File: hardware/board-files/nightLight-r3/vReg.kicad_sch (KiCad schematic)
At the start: 15 parts, among them IC1 PAM2401SCADJ, Q1 NMOS, Q2 PMOS

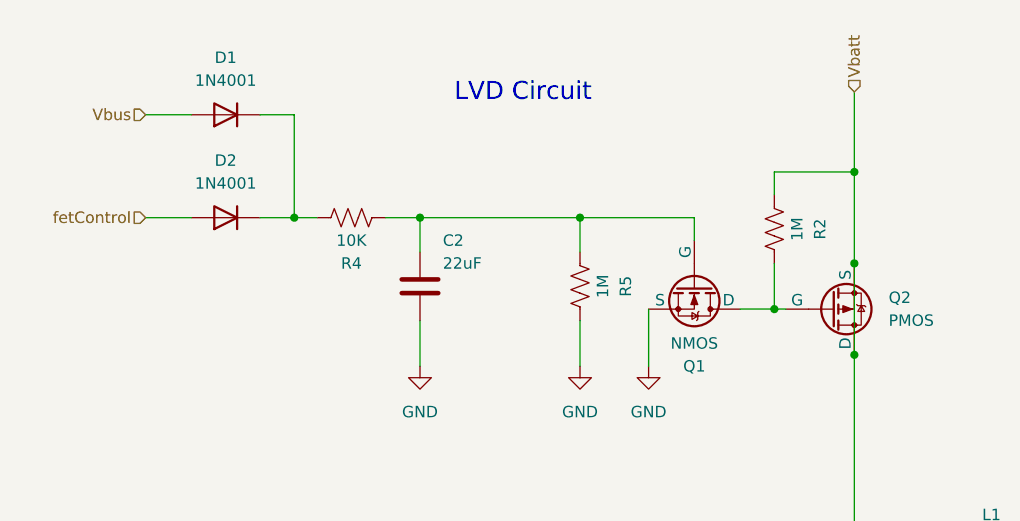
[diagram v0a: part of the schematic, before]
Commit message: finished shematic and added to PCB
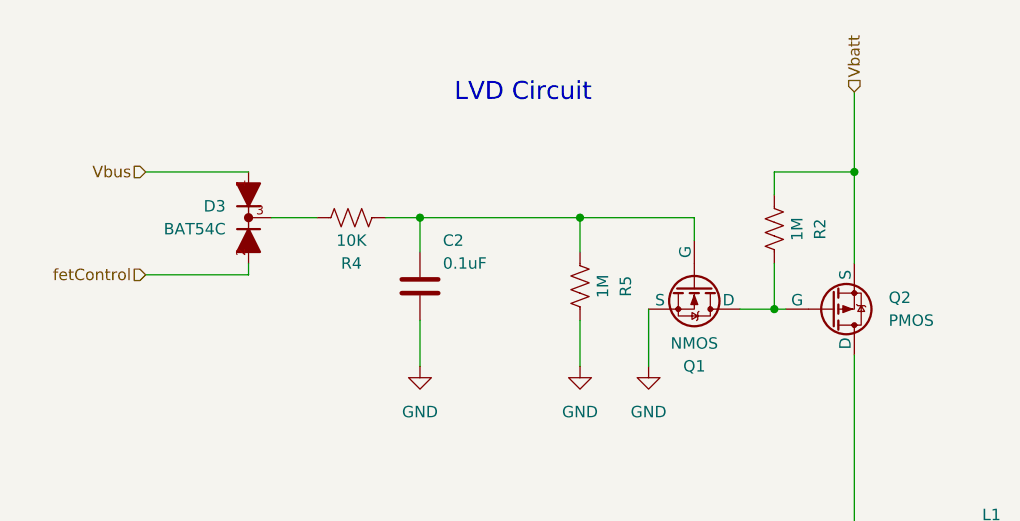
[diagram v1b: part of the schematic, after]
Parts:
- removed D1, D2: 1N4001, Diode_THT:D_DO-41_SOD81_P10.16mm_Horizontal, symbol Diode:1N4001
- added D3: BAT54C, BAT54C:SOT23-R, symbol BAT54C:BAT54C
- C2: value 22uF -> 0.1uF
- Q1: footprint (none) -> IRLML6402TRPBF:SOT95P237X112-3N
- Q2: footprint (none) -> IRLML6344TRPBF:SOT95P240X112-3N
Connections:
- net Vbatt: no longer C1.1, IC1.3 (VIN), L1.1, Q2.1 (D), R1.1
- net Vbus: now also D3.1
- net fetControl: now also D3.2
- net at R4.2: now also D3.3
- new net: C1.1, IC1.3 (VIN), L1.1, Q2.1 (D), R1.1
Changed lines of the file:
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@@
   (junction (at 115.57 71.12) (diameter 0) (color 0 0 0 0)
   )
-  (junction (at 83.82 71.12) (diameter 0) (color 0 0 0 0)
-  )
   (junction (at 97.79 71.12) (diameter 0) (color 0 0 0 0)
   )
@@
   (junction (at 146.05 66.04) (diameter 0) (color 0 0 0 0)
   )
-  (junction (at 146.05 76.2) (diameter 0) (color 0 0 0 0)
-  )
   (junction (at 146.05 127) (diameter 0) (color 0 0 0 0)
   )
@@
   )
   (junction (at 151.13 127) (diameter 0) (color 0 0 0 0)
-  )
-  (junction (at 146.05 86.36) (diameter 0) (color 0 0 0 0)
   )
   (junction (at 208.28 129.54) (diameter 0) (color 0 0 0 0)
@@
     (stroke (width 0) (type default))
   )
-  (wire (pts (xy 80.01 59.69) (xy 83.82 59.69))
-    (stroke (width 0) (type default))
-  )
   (wire (pts (xy 137.16 76.2) (xy 137.16 81.28))
     (stroke (width 0) (type default))
@@
     (stroke (width 0) (type default))
   )
-  (wire (pts (xy 67.31 59.69) (xy 72.39 59.69))
+  (wire (pts (xy 67.31 66.04) (xy 78.74 66.04))
     (stroke (width 0) (type default))
   )
@@
     (stroke (width 0) (type default))
   )
-  (wire (pts (xy 67.31 71.12) (xy 72.39 71.12))
+  (wire (pts (xy 78.74 77.47) (xy 78.74 76.2))
+    (stroke (width 0) (type default))
+  )
+  (wire (pts (xy 67.31 77.47) (xy 78.74 77.47))
     (stroke (width 0) (type default))
   )
@@
     (stroke (width 0) (type default))
   )
-  (wire (pts (xy 146.05 76.2) (xy 146.05 86.36))
-    (stroke (width 0) (type default))
-  )
   (wire (pts (xy 146.05 66.04) (xy 146.05 76.2))
     (stroke (width 0) (type default))
@@
     (stroke (width 0) (type default))
   )
-  (wire (pts (xy 83.82 71.12) (xy 86.36 71.12))
-    (stroke (width 0) (type default))
-  )
   (wire (pts (xy 208.28 127) (xy 208.28 129.54))
     (stroke (width 0) (type default))
@@
     (stroke (width 0) (type default))
   )
-  (wire (pts (xy 83.82 59.69) (xy 83.82 71.12))
-    (stroke (width 0) (type default))
-  )
   (wire (pts (xy 146.05 86.36) (xy 146.05 127))
     (stroke (width 0) (type default))
@@
     (stroke (width 0) (type default))
   )
-  (wire (pts (xy 83.82 71.12) (xy 80.01 71.12))
+  (wire (pts (xy 81.28 71.12) (xy 86.36 71.12))
     (stroke (width 0) (type default))
   )
@@
     (effects (font (size 2 2) (color 237 0 0 1)) (justify left bottom))
   )
-  (hierarchical_label "fetControl" (shape input) (at 67.31 71.12 180) (fields_autoplaced)
+  (hierarchical_label "fetControl" (shape input) (at 67.31 77.47 180) (fields_autoplaced)
     (effects (font (size 1.27 1.27)) (justify right))
   )
-  (hierarchical_label "Vbus" (shape input) (at 67.31 59.69 180) (fields_autoplaced)
+  (hierarchical_label "Vbus" (shape input) (at 67.31 66.04 180) (fields_autoplaced)
     (effects (font (size 1.27 1.27)) (justify right))
   )
@@
     )
   )
-  (netclass_flag "" (length 2.54) (shape dot) (at 83.82 64.77 270) (fields_autoplaced)
-    (effects (font (size 1.27 1.27)) (justify right bottom))
-    (property "Netclass" "signal" (at 86.36 64.0715 90)
+  (netclass_flag "" (length 2.54) (shape dot) (at 83.82 71.12 0) (fields_autoplaced)
+    (effects (font (size 1.27 1.27)) (justify left bottom))
+    (property "Netclass" "signal" (at 84.5185 68.58 0)
       (effects (font (size 1.27 1.27) italic) (justify left) hide)
     )
@@
       (effects (font (size 1.27 1.27)))
     )
-    (property "Footprint" "" (at 130.81 83.82 0)
+    (property "Footprint" "IRLML6402TRPBF:SOT95P237X112-3N" (at 130.81 83.82 0)
       (effects (font (size 1.27 1.27)) hide)
     )
@@
     )
   )
+  (symbol (lib_id "BAT54C:BAT54C") (at 78.74 71.12 0) (unit 1)
+    (in_bom yes) (on_board yes) (dnp no) (fields_autoplaced)
+    (property "Reference" "D3" (at 76.2 69.85 0)
+      (effects (font (size 1.27 1.27)) (justify right))
+    )
+    (property "Value" "BAT54C" (at 76.2 72.39 0)
+      (effects (font (size 1.27 1.27)) (justify right))
+    )
+    (property "Footprint" "BAT54C:SOT23-R" (at 78.74 71.12 0)
+      (effects (font (size 1.27 1.27)) (justify bottom) hide)
+    )
+    (property "Datasheet" "" (at 78.74 71.12 0)
+      (effects (font (size 1.27 1.27)) hide)
+    )
+    (property "MF" "Diotec Semiconductor" (at 78.74 71.12 0)
+      (effects (font (size 1.27 1.27)) (justify bottom) hide)
+    )
+    (property "Description" "\n                        \n                            Schottky, SOT-23, 30V, 0.2A, 150°C\n                        \n" (at 78.74 71.12 0)
+      (effects (font (size 1.27 1.27)) (justify bottom) hide)
+    )
+    (property "Package" "SOT-23 Diotec" (at 78.74 71.12 0)
+      (effects (font (size 1.27 1.27)) (justify bottom) hide)
+    )
+    (property "Price" "None" (at 78.74 71.12 0)
+      (effects (font (size 1.27 1.27)) (justify bottom) hide)
+    )
+    (property "SnapEDA_Link" "https://www.snapeda.com/parts/BAT54C/Diotec/view-part/?ref=snap" (at 78.74 71.12 0)
+      (effects (font (size 1.27 1.27)) (justify bottom) hide)
+    )
+    (property "MP" "BAT54C" (at 78.74 71.12 0)
+      (effects (font (size 1.27 1.27)) (justify bottom) hide)
+    )
+    (property "Availability" "In Stock" (at 78.74 71.12 0)
+      (effects (font (size 1.27 1.27)) (justify bottom) hide)
+    )
+    (property "Check_prices" "https://www.snapeda.com/parts/BAT54C/Diotec/view-part/?ref=eda" (at 78.74 71.12 0)
+      (effects (font (size 1.27 1.27)) (justify bottom) hide)
+    )
+    (pin "1")
+    (pin "3")
+    (pin "2")
+    (instances
+      (project "nightLight"
+        (path "/203033dd-6a13-4262-9a98-8b29445e90e8/e6a767d4-c228-4ec6-8577-23f8c70359e3"
+          (reference "D3") (unit 1)
+        )
+      )
+    )
+  )
   (symbol (lib_id "Device:C") (at 97.79 78.74 0) (unit 1)
     (in_bom yes) (on_board yes) (dnp no)
@@
       (effects (font (size 1.27 1.27)) (justify left))
     )
-    (property "Value" "22uF" (at 100.33 76.2 0)
+    (property "Value" "0.1uF" (at 100.33 76.2 0)
       (effects (font (size 1.27 1.27)) (justify left))
     )
@@
       (effects (font (size 1.27 1.27)) (justify left))
     )
-    (property "Footprint" "" (at 148.59 83.82 0)
+    (property "Footprint" "IRLML6344TRPBF:SOT95P240X112-3N" (at 148.59 83.82 0)
       (effects (font (size 1.27 1.27)) hide)
     )
@@
     )
   )
-  (symbol (lib_id "Diode:1N4001") (at 76.2 71.12 180) (unit 1)
-    (in_bom yes) (on_board yes) (dnp no) (fields_autoplaced)
-    (property "Reference" "D2" (at 76.2 64.77 0)
-      (effects (font (size 1.27 1.27)))
-    )
-    (property "Value" "1N4001" (at 76.2 67.31 0)
-      (effects (font (size 1.27 1.27)))
-    )
-    (property "Footprint" "Diode_THT:D_DO-41_SOD81_P10.16mm_Horizontal" (at 76.2 71.12 0)
-      (effects (font (size 1.27 1.27)) hide)
-    )
-    (property "Datasheet" "http://www.vishay.com/docs/88503/1n4001.pdf" (at 76.2 71.12 0)
-      (effects (font (size 1.27 1.27)) hide)
-    )
-    (property "Sim.Device" "D" (at 76.2 71.12 0)
-      (effects (font (size 1.27 1.27)) hide)
-    )
-    (property "Sim.Pins" "1=K 2=A" (at 76.2 71.12 0)
-      (effects (font (size 1.27 1.27)) hide)
-    )
-    (pin "1")
-    (pin "2")
-    (instances
-      (project "nightLight"
-        (path "/203033dd-6a13-4262-9a98-8b29445e90e8/e6a767d4-c228-4ec6-8577-23f8c70359e3"
-          (reference "D2") (unit 1)
-        )
-      )
-    )
-  )
   (symbol (lib_id "power:GND") (at 218.44 139.7 0) (unit 1)
     (in_bom yes) (on_board yes) (dnp no) (fields_autoplaced)
@@
         )
       )
-    )
-  )
-  (symbol (lib_id "Diode:1N4001") (at 76.2 59.69 180) (unit 1)
-    (in_bom yes) (on_board yes) (dnp no) (fields_autoplaced)
-    (property "Reference" "D1" (at 76.2 53.34 0)
-      (effects (font (size 1.27 1.27)))
-    )
-    (property "Value" "1N4001" (at 76.2 55.88 0)
-      (effects (font (size 1.27 1.27)))
-    )
-    (property "Footprint" "Diode_THT:D_DO-41_SOD81_P10.16mm_Horizontal" (at 76.2 59.69 0)
-      (effects (font (size 1.27 1.27)) hide)
-    )
-    (property "Datasheet" "http://www.vishay.com/docs/88503/1n4001.pdf" (at 76.2 59.69 0)
-      (effects (font (size 1.27 1.27)) hide)
-    )
-    (property "Sim.Device" "D" (at 76.2 59.69 0)
-      (effects (font (size 1.27 1.27)) hide)
-    )
-    (property "Sim.Pins" "1=K 2=A" (at 76.2 59.69 0)
-      (effects (font (size 1.27 1.27)) hide)
-    )
-    (pin "1")
-    (pin "2")
-    (instances
-      (project "nightLight"
-        (path "/203033dd-6a13-4262-9a98-8b29445e90e8/e6a767d4-c228-4ec6-8577-23f8c70359e3"
-          (reference "D1") (unit 1)
-        )
-      )

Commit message: first layout revision
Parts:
- renumbered C2 to C1, C3 to C2, C1 to C3, D3 to D1, R4 to R1, R5 to R3, R1 to R4, R3 to R5, R7 to R6

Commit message: PCB rev 3.1 done
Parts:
- removed Q1: NMOS, IRLML6402TRPBF:SOT95P237X112-3N, symbol Simulation_SPICE:NMOS
- removed Q2: PMOS, IRLML6344TRPBF:SOT95P240X112-3N, symbol Simulation_SPICE:PMOS
- added Q1: AO3400A, Package_TO_SOT_SMD:SOT-23, symbol Transistor_FET:AO3400A
- added Q2: AO3401A, Package_TO_SOT_SMD:SOT-23, symbol Transistor_FET:AO3401A
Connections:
- net GND: now also Q1.2 (S)
- net Vbatt: now also Q2.3 (D)
- net at C3.1, IC1.3 (VIN), L1.1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: now also Q2.2 (S)
- net at C1.1, R1.1, R3.1: now also Q1.1 (G)
- net at R2.2: now also Q1.3 (D), Q2.1 (G)
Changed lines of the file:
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@@
   (junction (at 146.05 66.04) (diameter 0) (color 0 0 0 0)
   )
+  (junction (at 137.16 78.74) (diameter 0) (color 0 0 0 0)
+  )
   (junction (at 146.05 127) (diameter 0) (color 0 0 0 0)
   )
   (junction (at 151.13 119.38) (diameter 0) (color 0 0 0 0)
-  )
-  (junction (at 137.16 81.28) (diameter 0) (color 0 0 0 0)
   )
   (junction (at 151.13 127) (diameter 0) (color 0 0 0 0)
@@
     (stroke (width 0) (type default))
   )
-  (wire (pts (xy 137.16 76.2) (xy 137.16 81.28))
+  (wire (pts (xy 137.16 76.2) (xy 137.16 78.74))
+    (stroke (width 0) (type default))
+  )
+  (wire (pts (xy 134.62 78.74) (xy 137.16 78.74))
     (stroke (width 0) (type default))
   )
@@
     (stroke (width 0) (type default))
   )
-  (wire (pts (xy 115.57 71.12) (xy 128.27 71.12))
-    (stroke (width 0) (type default))
-  )
-  (wire (pts (xy 146.05 66.04) (xy 146.05 76.2))
+  (wire (pts (xy 146.05 66.04) (xy 146.05 73.66))
     (stroke (width 0) (type default))
   )
@@
     (stroke (width 0) (type default))
   )
+  (wire (pts (xy 137.16 78.74) (xy 138.43 78.74))
+    (stroke (width 0) (type default))
+  )
   (wire (pts (xy 218.44 127) (xy 218.44 139.7))
     (stroke (width 0) (type default))
@@
     (stroke (width 0) (type default))
   )
-  (wire (pts (xy 137.16 81.28) (xy 138.43 81.28))
-    (stroke (width 0) (type default))
-  )
   (wire (pts (xy 151.13 119.38) (xy 157.48 119.38))
     (stroke (width 0) (type default))
@@
     (stroke (width 0) (type default))
   )
+  (wire (pts (xy 124.46 78.74) (xy 123.19 78.74))
+    (stroke (width 0) (type default))
+  )
+  (wire (pts (xy 115.57 71.12) (xy 129.54 71.12))
+    (stroke (width 0) (type default))
+  )
   (wire (pts (xy 171.45 116.84) (xy 168.91 116.84))
     (stroke (width 0) (type default))
   )
-  (wire (pts (xy 146.05 86.36) (xy 146.05 127))
+  (wire (pts (xy 146.05 83.82) (xy 146.05 127))
     (stroke (width 0) (type default))
   )
@@
     (stroke (width 0) (type default))
   )
-  (wire (pts (xy 133.35 81.28) (xy 137.16 81.28))
-    (stroke (width 0) (type default))
-  )
   (wire (pts (xy 146.05 57.15) (xy 146.05 66.04))
     (stroke (width 0) (type default))
@@
     (stroke (width 0) (type default))
   )
-  (wire (pts (xy 123.19 81.28) (xy 123.19 87.63))
+  (wire (pts (xy 123.19 78.74) (xy 123.19 87.63))
     (stroke (width 0) (type default))
   )
@@
   )
   (wire (pts (xy 151.13 110.49) (xy 151.13 119.38))
-    (stroke (width 0) (type default))
-  )
-  (wire (pts (xy 128.27 71.12) (xy 128.27 73.66))
     (stroke (width 0) (type default))
   )
@@
         (path "/203033dd-6a13-4262-9a98-8b29445e90e8/e6a767d4-c228-4ec6-8577-23f8c70359e3"
           (reference "R2") (unit 1)
+        )
+      )
+    )
+  )
+  (symbol (lib_id "Transistor_FET:AO3400A") (at 129.54 76.2 270) (unit 1)
+    (in_bom yes) (on_board yes) (dnp no) (fields_autoplaced)
+    (property "Reference" "Q1" (at 129.54 82.55 90)
+      (effects (font (size 1.27 1.27)))
+    )
+    (property "Value" "AO3400A" (at 129.54 85.09 90)
+      (effects (font (size 1.27 1.27)))
+    )
+    (property "Footprint" "Package_TO_SOT_SMD:SOT-23" (at 127.635 81.28 0)
+      (effects (font (size 1.27 1.27) italic) (justify left) hide)
+    )
+    (property "Datasheet" "http://www.aosmd.com/pdfs/datasheet/AO3400A.pdf" (at 125.73 81.28 0)
+      (effects (font (size 1.27 1.27)) (justify left) hide)
+    )
+    (pin "3")
+    (pin "1")
+    (pin "2")
+    (instances
+      (project "nightLight"
+        (path "/203033dd-6a13-4262-9a98-8b29445e90e8/e6a767d4-c228-4ec6-8577-23f8c70359e3"
+          (reference "Q1") (unit 1)
         )
       )
@@
     )
   )
+  (symbol (lib_id "Transistor_FET:AO3401A") (at 143.51 78.74 0) (unit 1)
+    (in_bom yes) (on_board yes) (dnp no) (fields_autoplaced)
+    (property "Reference" "Q2" (at 149.86 77.47 0)
+      (effects (font (size 1.27 1.27)) (justify left))
+    )
+    (property "Value" "AO3401A" (at 149.86 80.01 0)
+      (effects (font (size 1.27 1.27)) (justify left))
+    )
+    (property "Footprint" "Package_TO_SOT_SMD:SOT-23" (at 148.59 80.645 0)
+      (effects (font (size 1.27 1.27) italic) (justify left) hide)
+    )
+    (property "Datasheet" "http://www.aosmd.com/pdfs/datasheet/AO3401A.pdf" (at 148.59 82.55 0)
+      (effects (font (size 1.27 1.27)) (justify left) hide)
+    )
+    (pin "3")
+    (pin "2")
+    (pin "1")
+    (instances
+      (project "nightLight"
+        (path "/203033dd-6a13-4262-9a98-8b29445e90e8/e6a767d4-c228-4ec6-8577-23f8c70359e3"
+          (reference "Q2") (unit 1)
+        )
+      )
+    )
+  )
   (symbol (lib_id "power:GND") (at 123.19 87.63 0) (unit 1)
     (in_bom yes) (on_board yes) (dnp no) (fields_autoplaced)
@@
         (path "/203033dd-6a13-4262-9a98-8b29445e90e8/e6a767d4-c228-4ec6-8577-23f8c70359e3"
           (reference "#PWR03") (unit 1)
-        )
-      )
-    )
-  )
-  (symbol (lib_id "Simulation_SPICE:NMOS") (at 128.27 78.74 270) (unit 1)
-    (in_bom yes) (on_board yes) (dnp no)
-    (property "Reference" "Q1" (at 128.27 87.63 90)
-      (effects (font (size 1.27 1.27)))
-    )
-    (property "Value" "NMOS" (at 128.27 85.09 90)
-      (effects (font (size 1.27 1.27)))
-    )
-    (property "Footprint" "IRLML6402TRPBF:SOT95P237X112-3N" (at 130.81 83.82 0)
-      (effects (font (size 1.27 1.27)) hide)
-    )
-    (property "Datasheet" "https://ngspice.sourceforge.io/docs/ngspice-html-manual/manual.xhtml#cha_MOSFETs" (at 115.57 78.74 0)
-      (effects (font (size 1.27 1.27)) hide)
-    )
-    (property "Sim.Device" "NMOS" (at 111.125 78.74 0)
-      (effects (font (size 1.27 1.27)) hide)
-    )
-    (property "Sim.Type" "VDMOS" (at 109.22 78.74 0)
-      (effects (font (size 1.27 1.27)) hide)
-    )
-    (property "Sim.Pins" "1=D 2=G 3=S" (at 113.03 78.74 0)
-      (effects (font (size 1.27 1.27)) hide)
-    )
-    (pin "1")
-    (pin "2")
-    (pin "3")
-    (instances
-      (project "nightLight"
-        (path "/203033dd-6a13-4262-9a98-8b29445e90e8/e6a767d4-c228-4ec6-8577-23f8c70359e3"
-          (reference "Q1") (unit 1)
         )
       )
@@
         )
       )
-    )
-  )
-  (symbol (lib_id "Simulation_SPICE:PMOS") (at 143.51 81.28 0) (mirror x) (unit 1)
-    (in_bom yes) (on_board yes) (dnp no)
-    (property "Reference" "Q2" (at 149.86 80.01 0)
-      (effects (font (size 1.27 1.27)) (justify left))
-    )
-    (property "Value" "PMOS" (at 149.86 82.55 0)
-      (effects (font (size 1.27 1.27)) (justify left))
-    )
-    (property "Footprint" "IRLML6344TRPBF:SOT95P240X112-3N" (at 148.59 83.82 0)
-      (effects (font (size 1.27 1.27)) hide)
-    )
-    (property "Datasheet" "https://ngspice.sourceforge.io/docs/ngspice-html-manual/manual.xhtml#cha_MOSFETs" (at 143.51 68.58 0)
-      (effects (font (size 1.27 1.27)) hide)
-    )
-    (property "Sim.Device" "PMOS" (at 143.51 64.135 0)
-      (effects (font (size 1.27 1.27)) hide)
-    )
-    (property "Sim.Type" "VDMOS" (at 143.51 62.23 0)
-      (effects (font (size 1.27 1.27)) hide)
-    )
-    (property "Sim.Pins" "1=D 2=G 3=S" (at 143.51 66.04 0)
-      (effects (font (size 1.27 1.27)) hide)
-    )
-    (pin "2")
-    (pin "3")
-    (pin "1")
-    (instances
-      (project "nightLight"
-        (path "/203033dd-6a13-4262-9a98-8b29445e90e8/e6a767d4-c228-4ec6-8577-23f8c70359e3"
-          (reference "Q2") (unit 1)
-        )
-      )
